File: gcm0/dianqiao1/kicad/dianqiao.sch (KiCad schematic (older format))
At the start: 73 parts, among them J1 Conn_Coaxial, J2 Conn_Coaxial, J3 Conn_Coaxial, J4 Conn_Coaxial, SW1 SW_Push, SW2 SW_Push, SW3 SW_Push, U1 NE5532, U10 TL084, U12 NE5532, U2 LM2596T-ADJ, U3 LM1117-3.3, U4 LM7805_TO220, U5 STM32F030F4P6, U6 CD4052B, U7 NE5532, U8 CD4053B, U9 74HC595, Y1 8M

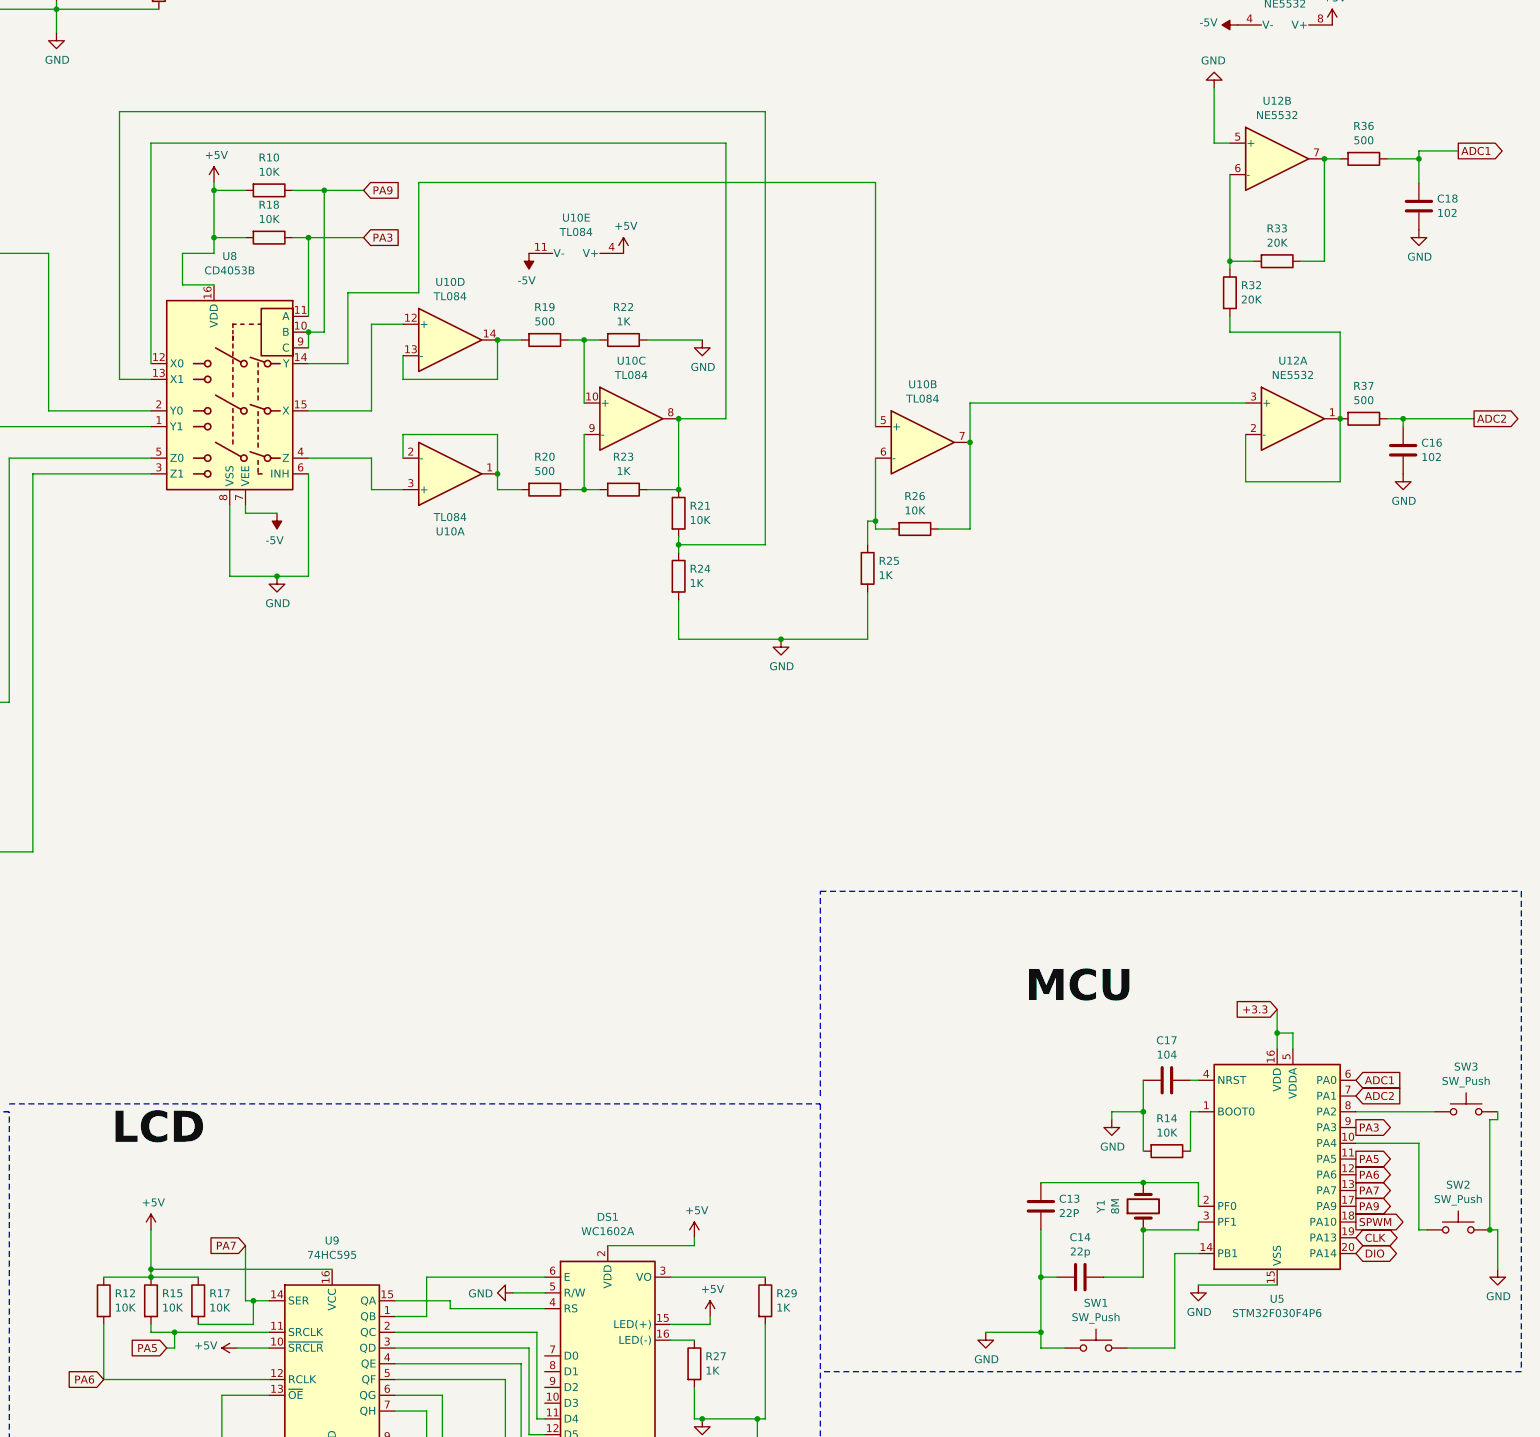
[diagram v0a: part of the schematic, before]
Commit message: 编写按键和菜单
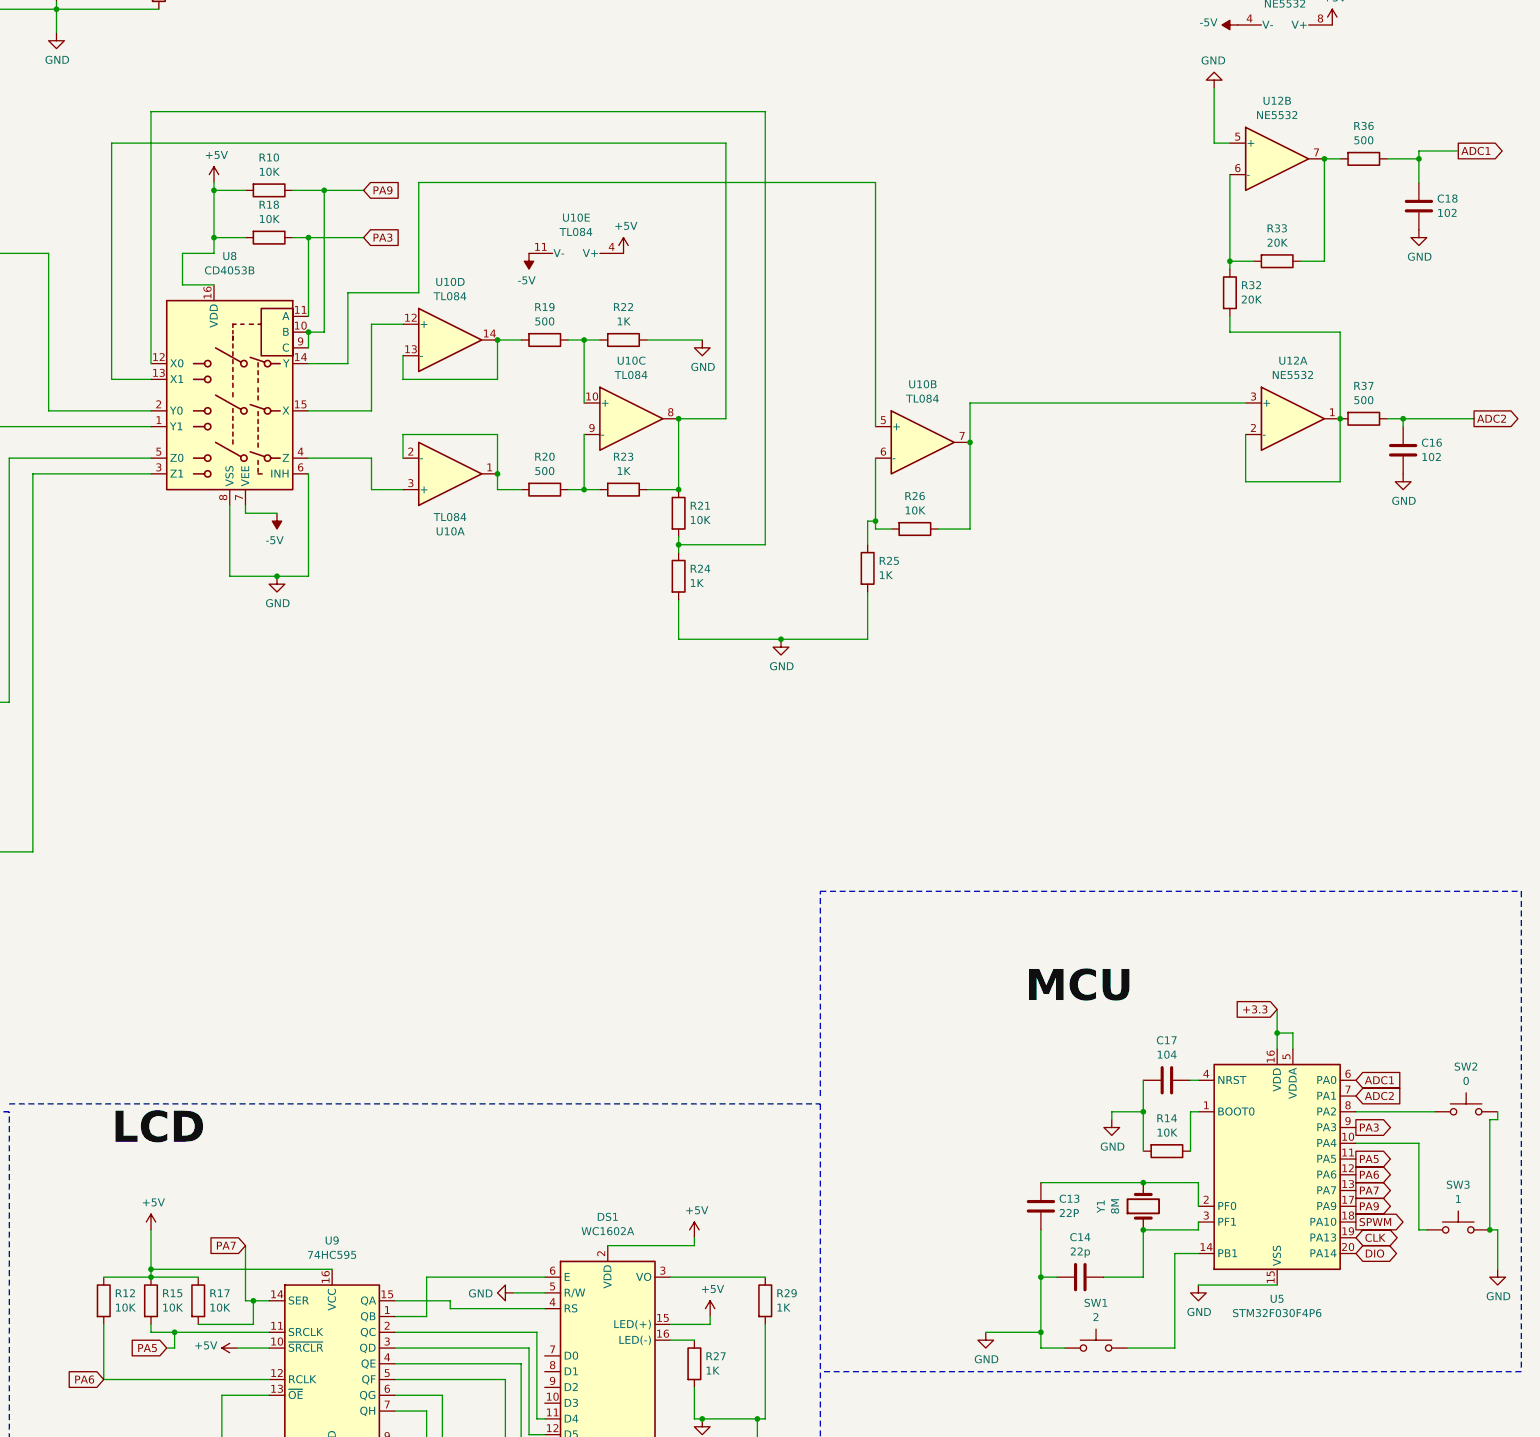
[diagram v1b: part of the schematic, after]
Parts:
- SW1: value SW_Push -> 2
- SW2: renamed from SW3; value SW_Push -> 0
- SW3: renamed from SW2; value SW_Push -> 1
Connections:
- net at R21.1, R23.1, U10.8: now also U8.13 (X1); no longer U8.12 (X0)
- net at R21.2, R24.1: now also U8.12 (X0); no longer U8.13 (X1)
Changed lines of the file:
@@
 P 13300 9800
 F 0 "SW1" H 13300 10085 50  0000 C CNN
-F 1 "SW_Push" H 13300 9994 50  0000 C CNN
+F 1 "2" H 13300 9994 50  0000 C CNN
 F 2 "" H 13300 10000 50  0001 C CNN
 F 3 "~" H 13300 10000 50  0001 C CNN
@@
 Text GLabel 14950 8400 2    50   Output ~ 0
 PA3
-Wire Wire Line
-	7100 1950 11200 1950
-Wire Wire Line
-	7300 2150 10950 2150
-Wire Wire Line
-	7100 3650 7300 3650
-Wire Wire Line
-	7100 1950 7100 3650
-Wire Wire Line
-	7300 3550 7300 2150
 Text GLabel 14950 8900 2    50   Output ~ 0
 PA9
 $Comp
-L Switch:SW_Push SW2
+L Switch:SW_Push SW3
 U 1 1 5FD147ED
 P 15600 9050
-F 0 "SW2" H 15600 9335 50  0000 C CNN
-F 1 "SW_Push" H 15600 9244 50  0000 C CNN
+F 0 "SW3" H 15600 9335 50  0000 C CNN
+F 1 "1" H 15600 9244 50  0000 C CNN
 F 2 "" H 15600 9250 50  0001 C CNN
 F 3 "~" H 15600 9250 50  0001 C CNN
@@
 SPWM
 $Comp
-L Switch:SW_Push SW3
+L Switch:SW_Push SW2
 U 1 1 5FE584F9
 P 15650 8300
-F 0 "SW3" H 15650 8585 50  0000 C CNN
-F 1 "SW_Push" H 15650 8494 50  0000 C CNN
+F 0 "SW2" H 15650 8585 50  0000 C CNN
+F 1 "0" H 15650 8494 50  0000 C CNN
 F 2 "" H 15650 8500 50  0001 C CNN
 F 3 "~" H 15650 8500 50  0001 C CNN
@@
 	12950 8750 13600 8750
 Connection ~ 13600 8750
+Wire Wire Line
+	7050 2150 7050 3650
+Wire Wire Line
+	7050 3650 7300 3650
+Wire Wire Line
+	7050 2150 10950 2150
+Wire Wire Line
+	11200 1950 7300 1950
+Wire Wire Line
+	7300 1950 7300 3550
 $EndSCHEMATC
